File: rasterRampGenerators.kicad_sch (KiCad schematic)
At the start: 40 parts, among them J2 H_Sync, J3 V_Sync, Q1 2N7000, Q10 2N7000, Q11 2N7000, Q12 2N7000, Q13 2N7000, Q14 2N7000, Q15 2N7000, Q2 2N7000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

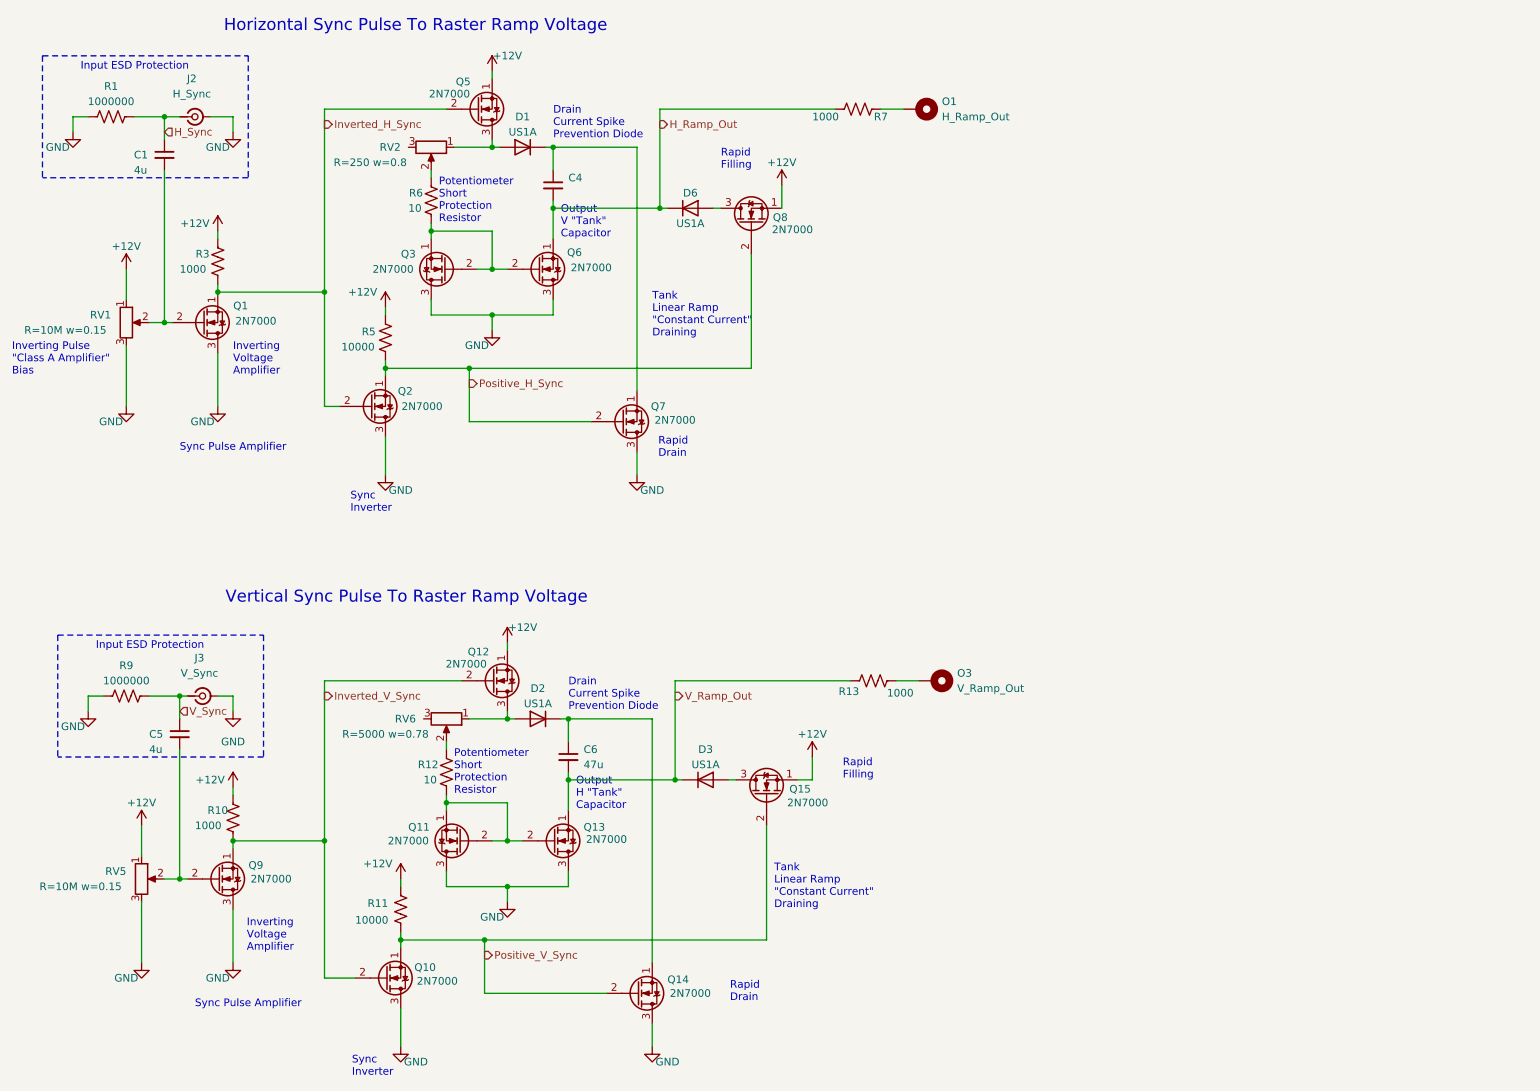
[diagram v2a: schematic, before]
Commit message: added sections to add to overview schematic, added some of the component schematics
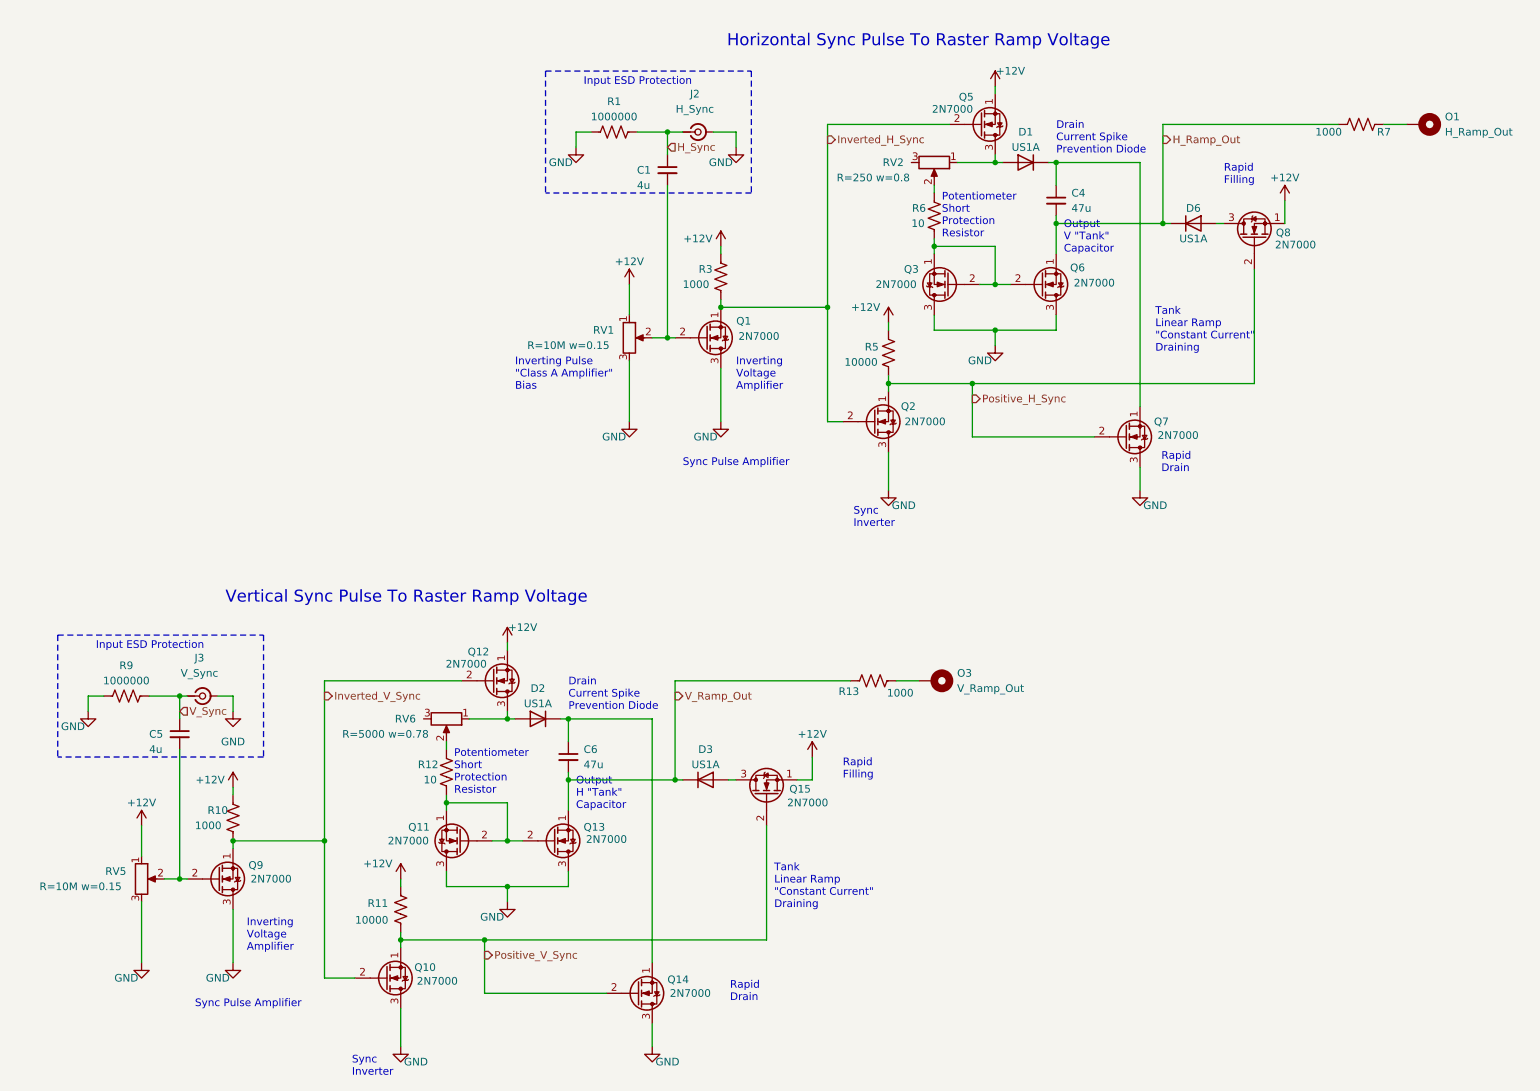
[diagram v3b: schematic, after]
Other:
- moved on the sheet: C1, C4, D1, D6, J2, O1, Q1, Q2, Q3, Q5, Q6, Q7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
